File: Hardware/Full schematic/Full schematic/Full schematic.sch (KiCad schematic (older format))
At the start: 111 parts, among them J1 Conn_01x04_Male, J2 Conn_01x04_Male, J3 Conn_01x02_Male, J4 Conn_01x02_Male, J5 Conn_01x02_Male, J6 Conn_01x02_Male, J7 Conn_01x02_Male, J8 Conn_01x06_Male, K1 EDR101A0500, K2 EDR101A0500, K3 EDR101A0500, K4 EDR101A0500, K5 EDR101A0500, Q1 BSS138, Q2 IRF610, Q3 IRLML2502, Q4 IRLML2502, Q5 IRLML2502, Q6 IRLML2502, Q7 IRLML2502, U1 74LVC2T45DC, U2 74LVC2T45DC, U3 AD9835, X1 50MHz

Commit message: After prototype built
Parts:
- C23: value 0.01uF -> 10nF
- K1, K2, K3, K4, K5: footprint Relay_THT:Relay_SPST_StandexMeder_MS_Form1AB -> Relay_THT:Relay_SPST_StandexMeder_SIL_Form1A
- U1, U2: footprint Package_SO:VSSOP-8_2.3x2mm_P0.5mm -> Package_SO:SSOP-8_3.9x5.05mm_P1.27mm
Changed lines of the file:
@@
 F 0 "U1" H 3100 1211 50  0000 C CNN
 F 1 "74LVC2T45DC" H 3100 1120 50  0000 C CNN
-F 2 "Package_SO:VSSOP-8_2.3x2mm_P0.5mm" H 3100 950 50  0001 C CNN
+F 2 "Package_SO:SSOP-8_3.9x5.05mm_P1.27mm" H 3100 950 50  0001 C CNN
 F 3 "https://assets.nexperia.com/documents/data-sheet/74LVC_LVCH2T45.pdf" H 3350 1550 50  0001 C CNN
 	1    3100 1800
@@
 F 0 "U2" H 3100 3061 50  0000 C CNN
 F 1 "74LVC2T45DC" H 3100 2970 50  0000 C CNN
-F 2 "Package_SO:VSSOP-8_2.3x2mm_P0.5mm" H 3100 2800 50  0001 C CNN
+F 2 "Package_SO:SSOP-8_3.9x5.05mm_P1.27mm" H 3100 2800 50  0001 C CNN
 F 3 "https://assets.nexperia.com/documents/data-sheet/74LVC_LVCH2T45.pdf" H 3350 3400 50  0001 C CNN
 	1    3100 3650
@@
 Wire Wire Line
 	12725 2200 12950 2200
-Wire Wire Line
-	13475 2250 13475 2200
 $Comp
 L power:GND #PWR055
@@
 P 13000 4050
 F 0 "C23" H 13115 4096 50  0000 L CNN
-F 1 "0.01uF" H 13115 4005 50  0000 L CNN
+F 1 "10nF" H 13115 4005 50  0000 L CNN
 F 2 "Capacitor_SMD:C_0805_2012Metric_Pad1.18x1.45mm_HandSolder" H 13038 3900 50  0001 C CNN
 F 3 "~" H 13000 4050 50  0001 C CNN
@@
 F 0 "K1" H 16075 3500 50  0000 R CNN
 F 1 "EDR101A0500" H 16100 3625 50  0000 R CNN
-F 2 "Relay_THT:Relay_SPST_StandexMeder_MS_Form1AB" H 16275 3700 50  0001 L CNN
+F 2 "Relay_THT:Relay_SPST_StandexMeder_SIL_Form1A" H 16275 3700 50  0001 L CNN
 F 3 "https://standexelectronics.com/de/produkte/ms-reed-relais/" H 15925 3750 50  0001 C CNN
 	1    15925 3750
@@
 F 0 "K2" H 17075 3500 50  0000 R CNN
 F 1 "EDR101A0500" H 17100 3625 50  0000 R CNN
-F 2 "Relay_THT:Relay_SPST_StandexMeder_MS_Form1AB" H 17275 3700 50  0001 L CNN
+F 2 "Relay_THT:Relay_SPST_StandexMeder_SIL_Form1A" H 17275 3700 50  0001 L CNN
 F 3 "https://standexelectronics.com/de/produkte/ms-reed-relais/" H 16925 3750 50  0001 C CNN
 	1    16925 3750
@@
 F 0 "K3" H 18075 3500 50  0000 R CNN
 F 1 "EDR101A0500" H 18100 3625 50  0000 R CNN
-F 2 "Relay_THT:Relay_SPST_StandexMeder_MS_Form1AB" H 18275 3700 50  0001 L CNN
+F 2 "Relay_THT:Relay_SPST_StandexMeder_SIL_Form1A" H 18275 3700 50  0001 L CNN
 F 3 "https://standexelectronics.com/de/produkte/ms-reed-relais/" H 17925 3750 50  0001 C CNN
 	1    17925 3750
@@
 F 0 "K4" H 19075 3500 50  0000 R CNN
 F 1 "EDR101A0500" H 19100 3625 50  0000 R CNN
-F 2 "Relay_THT:Relay_SPST_StandexMeder_MS_Form1AB" H 19275 3700 50  0001 L CNN
+F 2 "Relay_THT:Relay_SPST_StandexMeder_SIL_Form1A" H 19275 3700 50  0001 L CNN
 F 3 "https://standexelectronics.com/de/produkte/ms-reed-relais/" H 18925 3750 50  0001 C CNN
 	1    18925 3750
@@
 F 0 "K5" H 20075 3500 50  0000 R CNN
 F 1 "EDR101A0500" H 20100 3625 50  0000 R CNN
-F 2 "Relay_THT:Relay_SPST_StandexMeder_MS_Form1AB" H 20275 3700 50  0001 L CNN
+F 2 "Relay_THT:Relay_SPST_StandexMeder_SIL_Form1A" H 20275 3700 50  0001 L CNN
 F 3 "https://standexelectronics.com/de/produkte/ms-reed-relais/" H 19925 3750 50  0001 C CNN
 	1    19925 3750

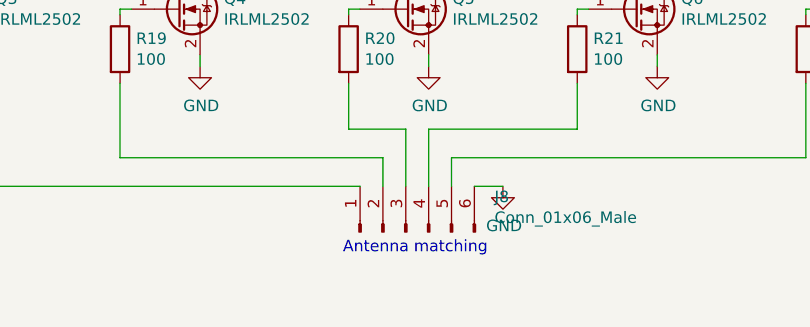
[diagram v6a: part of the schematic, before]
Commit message: Looks like 3.5MHz part is completely OK now
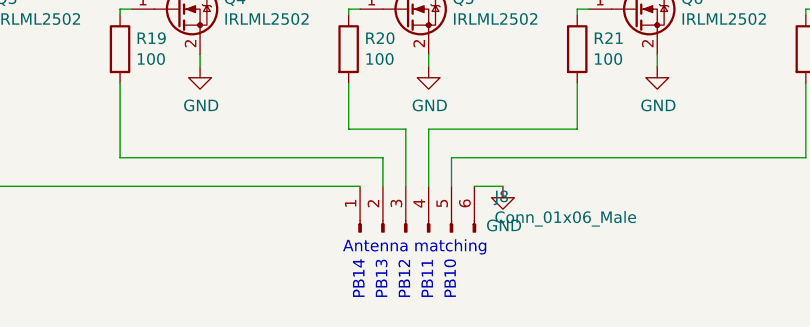
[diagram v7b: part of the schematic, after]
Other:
- note added: "PB10"
- note added: "PB11"
- note added: "PB12"
- note added: "PB13"
- note added: "PB14"
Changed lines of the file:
@@
 Wire Wire Line
 	10225 3725 10225 2700
+Text Notes 18250 5675 3    50   ~ 0
+PB10
+Text Notes 18150 5675 3    50   ~ 0
+PB11
+Text Notes 18050 5675 3    50   ~ 0
+PB12
+Text Notes 17950 5675 3    50   ~ 0
+PB13
+Text Notes 17850 5675 3    50   ~ 0
+PB14
 $EndSCHEMATC

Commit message: Added manipulation
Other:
- note added: "PB0"
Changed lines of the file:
@@
 Text Notes 17850 5675 3    50   ~ 0
 PB14
+Text Notes 8450 4050 0    50   ~ 0
+PB0
 $EndSCHEMATC
